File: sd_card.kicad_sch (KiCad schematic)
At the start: 11 parts, among them J5 SCHA5B0200

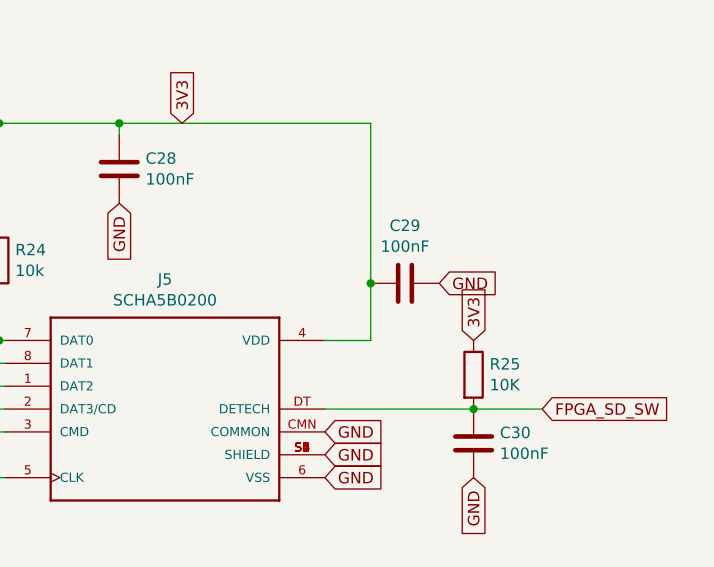
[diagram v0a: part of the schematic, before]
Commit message: Prod version of OpenAARS 5.0 design.
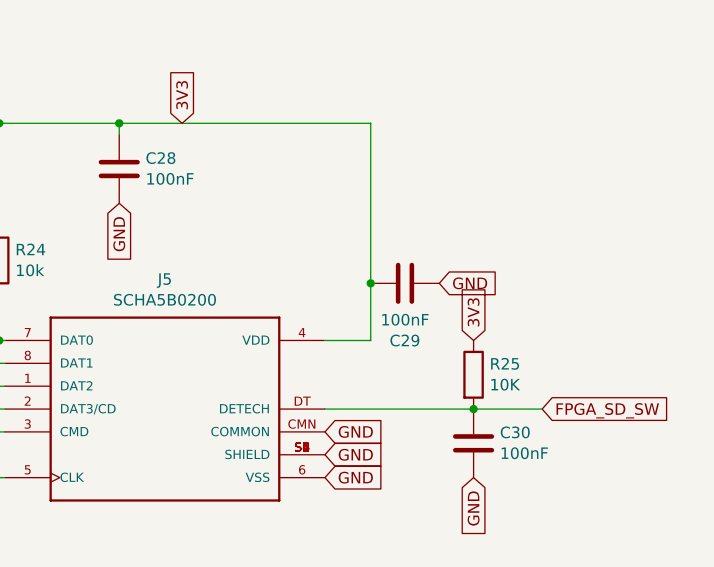
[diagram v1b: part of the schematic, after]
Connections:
- net 3V3: now also C29.1; no longer C29.2
- net GND: now also C29.2; no longer C29.1
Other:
- moved on the sheet: C29
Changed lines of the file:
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@@
   (junction (at 53.975 48.895) (diameter 0) (color 0 0 0 0)
   )
+  (junction (at 116.84 66.675) (diameter 0) (color 0 0 0 0)
+  )
   (junction (at 128.27 80.645) (diameter 0) (color 0 0 0 0)
   )
@@
   (junction (at 40.005 88.265) (diameter 0) (color 0 0 0 0)
   )
-  (junction (at 116.84 66.675) (diameter 0) (color 0 0 0 0)
-  )
   (junction (at 75.565 48.895) (diameter 0) (color 0 0 0 0)
   )
@@
     (stroke (width 0) (type default))
   )
+  (wire (pts (xy 116.84 48.895) (xy 116.84 66.675))
+    (stroke (width 0) (type default))
+  )
+  (wire (pts (xy 40.005 60.325) (xy 40.005 48.895))
+    (stroke (width 0) (type default))
+  )
+  (wire (pts (xy 88.9 48.895) (xy 116.84 48.895))
+    (stroke (width 0) (type default))
+  )
+  (wire (pts (xy 38.1 78.105) (xy 60.96 78.105))
+    (stroke (width 0) (type default))
+  )
+  (wire (pts (xy 53.975 48.895) (xy 53.975 60.325))
+    (stroke (width 0) (type default))
+  )
+  (polyline (pts (xy 12.065 12.065) (xy 153.035 12.065))
+    (stroke (width 0) (type default))
+  )
+  (wire (pts (xy 128.27 80.645) (xy 111.76 80.645))
+    (stroke (width 0) (type default))
+  )
+  (wire (pts (xy 60.96 78.105) (xy 76.2 78.105))
+    (stroke (width 0) (type default))
+  )
+  (wire (pts (xy 38.1 73.025) (xy 75.565 73.025))
+    (stroke (width 0) (type default))
+  )
+  (wire (pts (xy 46.99 48.895) (xy 53.975 48.895))
+    (stroke (width 0) (type default))
+  )
+  (wire (pts (xy 67.945 75.565) (xy 76.2 75.565))
+    (stroke (width 0) (type default))
+  )
+  (wire (pts (xy 135.89 80.645) (xy 128.27 80.645))
+    (stroke (width 0) (type default))
+  )
+  (wire (pts (xy 38.1 75.565) (xy 67.945 75.565))
+    (stroke (width 0) (type default))
+  )
+  (polyline (pts (xy 12.065 12.065) (xy 12.065 198.12))
+    (stroke (width 0) (type default))
+  )
+  (wire (pts (xy 40.005 67.945) (xy 40.005 88.265))
+    (stroke (width 0) (type default))
+  )
+  (wire (pts (xy 60.96 67.945) (xy 60.96 78.105))
+    (stroke (width 0) (type default))
+  )
+  (wire (pts (xy 46.99 60.325) (xy 46.99 48.895))
+    (stroke (width 0) (type default))
+  )
+  (wire (pts (xy 53.975 80.645) (xy 76.2 80.645))
+    (stroke (width 0) (type default))
+  )
+  (wire (pts (xy 53.975 48.895) (xy 60.96 48.895))
+    (stroke (width 0) (type default))
+  )
+  (wire (pts (xy 38.1 83.185) (xy 46.99 83.185))
+    (stroke (width 0) (type default))
+  )
+  (wire (pts (xy 75.565 48.895) (xy 88.9 48.895))
+    (stroke (width 0) (type default))
+  )
+  (wire (pts (xy 38.1 88.265) (xy 40.005 88.265))
+    (stroke (width 0) (type default))
+  )
+  (wire (pts (xy 46.99 83.185) (xy 76.2 83.185))
+    (stroke (width 0) (type default))
+  )
+  (polyline (pts (xy 153.035 198.12) (xy 12.065 198.12))
+    (stroke (width 0) (type default))
+  )
+  (wire (pts (xy 88.9 48.895) (xy 88.9 50.165))
+    (stroke (width 0) (type default))
+  )
+  (wire (pts (xy 46.99 67.945) (xy 46.99 83.185))
+    (stroke (width 0) (type default))
+  )
+  (wire (pts (xy 60.96 60.325) (xy 60.96 48.895))
+    (stroke (width 0) (type default))
+  )
+  (wire (pts (xy 75.565 60.325) (xy 75.565 48.895))
+    (stroke (width 0) (type default))
+  )
   (wire (pts (xy 116.84 66.675) (xy 116.84 73.025))
-    (stroke (width 0) (type default))
-  )
-  (wire (pts (xy 40.005 60.325) (xy 40.005 48.895))
-    (stroke (width 0) (type default))
-  )
-  (wire (pts (xy 88.9 48.895) (xy 116.84 48.895))
-    (stroke (width 0) (type default))
-  )
-  (wire (pts (xy 38.1 78.105) (xy 60.96 78.105))
-    (stroke (width 0) (type default))
-  )
-  (wire (pts (xy 53.975 48.895) (xy 53.975 60.325))
-    (stroke (width 0) (type default))
-  )
-  (polyline (pts (xy 12.065 12.065) (xy 153.035 12.065))
-    (stroke (width 0) (type default))
-  )
-  (wire (pts (xy 128.27 80.645) (xy 111.76 80.645))
-    (stroke (width 0) (type default))
-  )
-  (wire (pts (xy 60.96 78.105) (xy 76.2 78.105))
-    (stroke (width 0) (type default))
-  )
-  (wire (pts (xy 38.1 73.025) (xy 75.565 73.025))
-    (stroke (width 0) (type default))
-  )
-  (wire (pts (xy 46.99 48.895) (xy 53.975 48.895))
-    (stroke (width 0) (type default))
-  )
-  (wire (pts (xy 67.945 75.565) (xy 76.2 75.565))
-    (stroke (width 0) (type default))
-  )
-  (wire (pts (xy 135.89 80.645) (xy 128.27 80.645))
-    (stroke (width 0) (type default))
-  )
-  (wire (pts (xy 38.1 75.565) (xy 67.945 75.565))
-    (stroke (width 0) (type default))
-  )
-  (polyline (pts (xy 12.065 12.065) (xy 12.065 198.12))
-    (stroke (width 0) (type default))
-  )
-  (wire (pts (xy 40.005 67.945) (xy 40.005 88.265))
-    (stroke (width 0) (type default))
-  )
-  (wire (pts (xy 60.96 67.945) (xy 60.96 78.105))
-    (stroke (width 0) (type default))
-  )
-  (wire (pts (xy 46.99 60.325) (xy 46.99 48.895))
-    (stroke (width 0) (type default))
-  )
-  (wire (pts (xy 53.975 80.645) (xy 76.2 80.645))
-    (stroke (width 0) (type default))
-  )
-  (wire (pts (xy 53.975 48.895) (xy 60.96 48.895))
-    (stroke (width 0) (type default))
-  )
-  (wire (pts (xy 38.1 83.185) (xy 46.99 83.185))
-    (stroke (width 0) (type default))
-  )
-  (wire (pts (xy 75.565 48.895) (xy 88.9 48.895))
-    (stroke (width 0) (type default))
-  )
-  (wire (pts (xy 38.1 88.265) (xy 40.005 88.265))
-    (stroke (width 0) (type default))
-  )
-  (wire (pts (xy 46.99 83.185) (xy 76.2 83.185))
-    (stroke (width 0) (type default))
-  )
-  (polyline (pts (xy 153.035 198.12) (xy 12.065 198.12))
-    (stroke (width 0) (type default))
-  )
-  (wire (pts (xy 88.9 48.895) (xy 88.9 50.165))
-    (stroke (width 0) (type default))
-  )
-  (wire (pts (xy 46.99 67.945) (xy 46.99 83.185))
-    (stroke (width 0) (type default))
-  )
-  (wire (pts (xy 60.96 60.325) (xy 60.96 48.895))
-    (stroke (width 0) (type default))
-  )
-  (wire (pts (xy 75.565 60.325) (xy 75.565 48.895))
-    (stroke (width 0) (type default))
-  )
-  (wire (pts (xy 116.84 48.895) (xy 116.84 66.675))
     (stroke (width 0) (type default))
   )
@@
     )
   )
-  (symbol (lib_id "Device:C") (at 120.65 66.675 270) (unit 1)
-    (in_bom yes) (on_board yes) (dnp no)
-    (property "Reference" "C29" (at 120.65 60.2742 90)
+  (symbol (lib_id "Device:C") (at 120.65 66.675 90) (unit 1)
+    (in_bom yes) (on_board yes) (dnp no)
+    (property "Reference" "C29" (at 120.65 73.0758 90)
       (effects (font (size 1.27 1.27)))
     )
-    (property "Value" "100nF" (at 120.65 62.5856 90)
+    (property "Value" "100nF" (at 120.65 70.7644 90)
       (effects (font (size 1.27 1.27)))
     )
-    (property "Footprint" "Capacitor_SMD:C_0603_1608Metric" (at 116.84 67.6402 0)
-      (effects (font (size 1.27 1.27)) hide)
-    )
+    (property "Footprint" "Capacitor_SMD:C_0603_1608Metric" (at 124.46 65.7098 0)
+      (effects (font (size 1.27 1.27)) hide)
+    )
